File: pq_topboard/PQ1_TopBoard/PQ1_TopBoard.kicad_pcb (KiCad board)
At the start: 2 copper layers, 50 x 50 mm, 11 parts, among them IC1 TCN75AVUA713-VAO

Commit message: Functional revision and finishing touches part II
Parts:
- removed 11PICO: REF, easyeda:MOLEX_PICOBLADE_53261-1171_11X1.25MM_ANGLED
- removed PHT: SLCD-61N8, easyeda:SLCD-61N8
- removed R1, R2: 5k, easyeda:R0805
- added Annotation1: Silkscreen_Annotation, symbols-nsl:IEEE_logo, F.Cu at (102.9, 52.7)
- added Annotation2: Silkscreen_Annotation, symbols-nsl:GRSS, F.Cu at (119.5, 58.4)
- added Annotation3: Silkscreen_Annotation, symbols-nsl:NSL_long, F.Cu at (102.0, 36.1)
- added Annotation4: Silkscreen_Annotation, symbols-nsl:Telecos, F.Cu at (86.4, 58.0)
- added Annotation5: Silkscreen_Annotation, symbols-nsl:UPC_positiu, F.Cu at (102.5, 77.8)
- added C1: 1 uF, Capacitor_SMD:C_0603_1608Metric, B.Cu at (114.6, 61.1)
- added D1: SLCD-61N8, passive-nsl:SLCD-61N8, F.Cu at (102.7, 41.6)
- added H1: MountingHole_Pad, MountingHole:MountingHole_3.2mm_M3_ISO14580_Pad, F.Cu at (86.4, 41.7)
- added H2: MountingHole_Pad, MountingHole:MountingHole_3.2mm_M3_ISO14580_Pad, F.Cu at (119.3, 41.8)
- added H3: MountingHole_Pad, MountingHole:MountingHole_3.2mm_M3_ISO14580_Pad, F.Cu at (119.3, 74.8)
- added H4: MountingHole_Pad, MountingHole:MountingHole_3.2mm_M3_ISO14580_Pad, F.Cu at (86.3, 74.8)
- added H5: MountingHole, MountingHole:MountingHole_8.4mm_M8, F.Cu at (102.8, 65.2)
- added J1: Conn_01x11_MountingPin, Connector_Molex:Molex_PicoBlade_53261-0971_1x09-1MP_P1.25mm_Horizontal, B.Cu at (98.1, 52.1)
- GA0, GA1, GA2, VA0, VA1, VA2: value 5k -> 0R; footprint easyeda:R0805 -> Resistor_SMD:R_0805_2012Metric; moved to B.Cu
- IC1: value TCN75AVUA713-VAO -> TCN75AVUA713; footprint easyeda:SOP65P490X110-8N -> Package_SO:SOP-8_3.9x4.9mm_P1.27mm; moved to B.Cu
- moved IC1 9.58 mm to (112.0, 56.7), turned to 0 degrees
- moved VA0 8.28 mm to (115.3, 52.2), turned to 0 degrees
- moved GA2 6.81 mm to (108.9, 47.6), turned to 0 degrees
- moved VA1 5.05 mm to (115.3, 49.9), turned to 0 degrees
- moved GA1 3.71 mm to (109.0, 49.9), turned to 0 degrees
- moved VA2 2.02 mm to (115.3, 47.7), turned to 0 degrees
- moved GA0 1.65 mm to (109.0, 52.2), turned to 0 degrees
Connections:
- GA0 pad 1: (no net) -> GND
- GA0 pad 2: (no net) -> Net-(IC1-Pad7)
- GA1 pad 1: (no net) -> GND
- GA1 pad 2: (no net) -> Net-(IC1-Pad6)
- GA2 pad 1: (no net) -> GND
- GA2 pad 2: (no net) -> Net-(IC1-Pad5)
- IC1 pad 1: (no net) -> /SDA
- IC1 pad 2: (no net) -> /SCL
- IC1 pad 3: (no net) -> GND
- IC1 pad 4: (no net) -> GND
- IC1 pad 5: (no net) -> Net-(IC1-Pad5)
- IC1 pad 6: (no net) -> Net-(IC1-Pad6)
- IC1 pad 7: (no net) -> Net-(IC1-Pad7)
- IC1 pad 8: (no net) -> /VCC
- VA0 pad 1: (no net) -> Net-(IC1-Pad7)
- VA0 pad 2: (no net) -> /VCC
- VA1 pad 1: (no net) -> Net-(IC1-Pad6)
- VA1 pad 2: (no net) -> /VCC
- VA2 pad 1: (no net) -> Net-(IC1-Pad5)
- VA2 pad 2: (no net) -> /VCC
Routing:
- net (no net): track 166.2 -> 0.00 mm, vias 136 -> 0
- net Net-(IC1-Pad6): track 0.00 -> 23.2 mm
- net /PH+: track 0.00 -> 18.2 mm, vias 0 -> 1
- net /VCC: track 0.00 -> 16.2 mm
- net /PH-: track 0.00 -> 15.0 mm, vias 0 -> 1
- net Net-(IC1-Pad7): track 0.00 -> 14.9 mm
- net Net-(IC1-Pad5): track 0.00 -> 13.6 mm
- net /SDA: track 0.00 -> 13.6 mm
- net /SCL: track 0.00 -> 11.6 mm
- added copper zone on B.Cu, net GND
- added copper zone on F.Cu, net GND
- removed copper zone on B.Cu, net (none)
- removed copper zone on F.Cu, net (none)
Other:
- board text added: "TOP BOARD PQ1"
- board text removed: "TOP BOARD PL1"

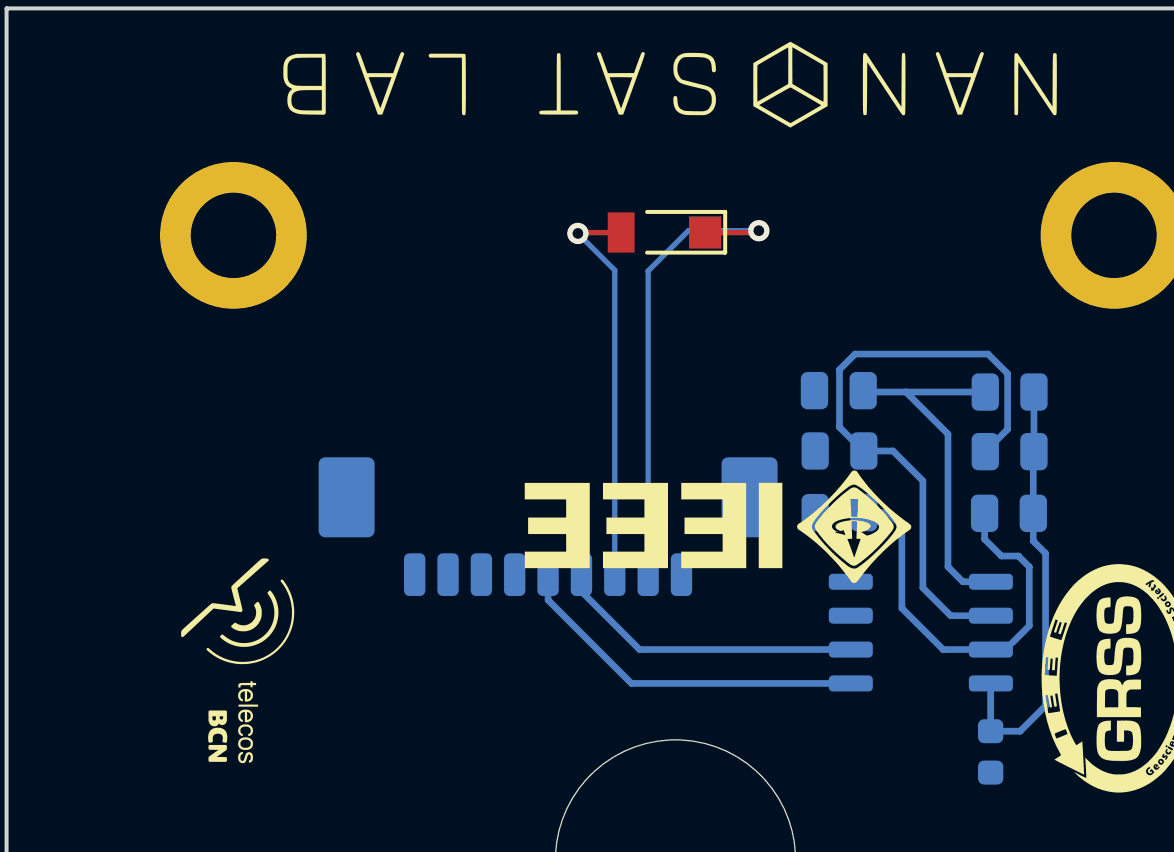
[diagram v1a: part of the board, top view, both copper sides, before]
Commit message: Full Kicad7 transition, library improvement and adaptation, correct footprints and 3D models added
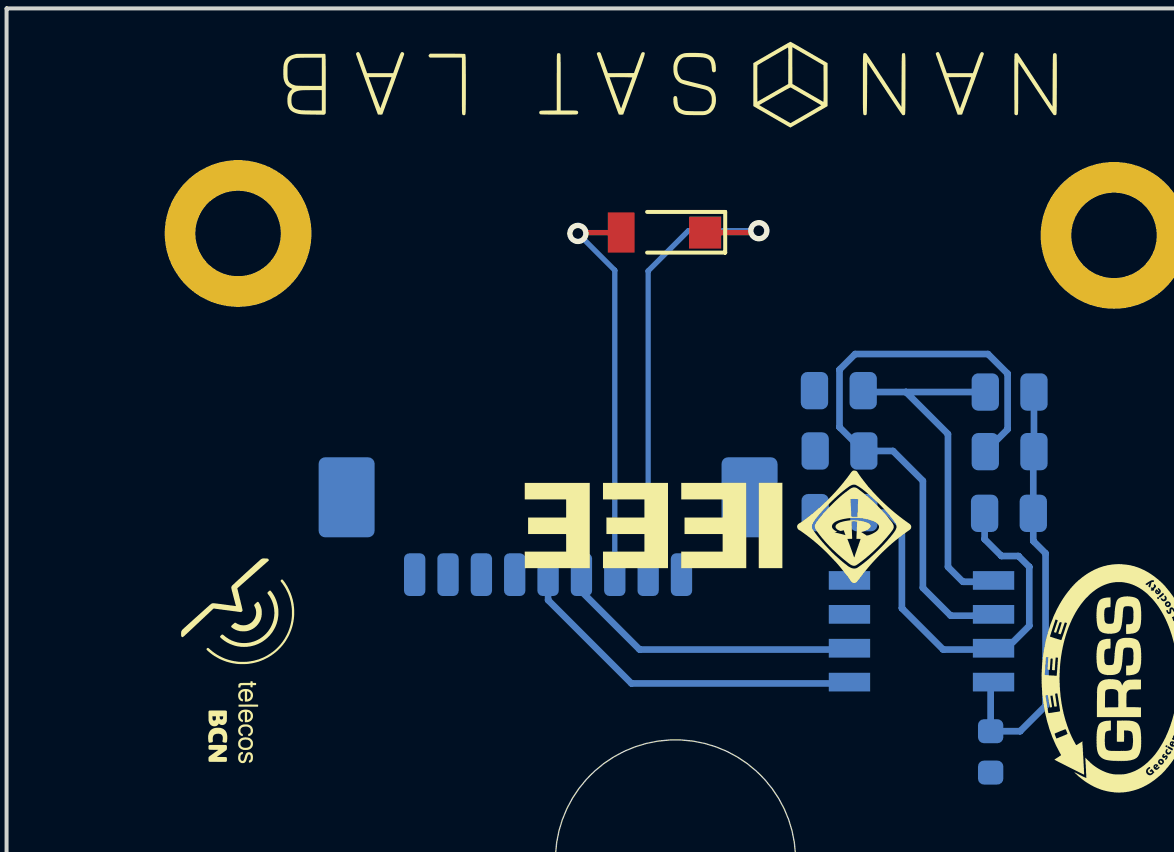
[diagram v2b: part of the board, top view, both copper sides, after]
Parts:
- Annotation1: footprint symbols-nsl:IEEE_logo -> -nsl_symbols:IEEE_logo
- Annotation2: footprint symbols-nsl:GRSS -> -nsl_symbols:GRSS
- Annotation3: footprint symbols-nsl:NSL_long -> -nsl_symbols:NSL_long
- Annotation4: footprint symbols-nsl:Telecos -> -nsl_symbols:Telecos
- Annotation5: footprint symbols-nsl:UPC_positiu -> -nsl_symbols:UPC_positiu
- D1: footprint passive-nsl:SLCD-61N8 -> -nsl_passive:SLCD-61N8
- IC1: footprint Package_SO:SOP-8_3.9x4.9mm_P1.27mm -> -nsl_sensor:TCN75AVOA
